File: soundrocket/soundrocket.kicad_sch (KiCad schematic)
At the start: 4 parts, among them J2 XLR3 MALE (OUT), U1 Teensy4.0, U3 CS8406-DSZ

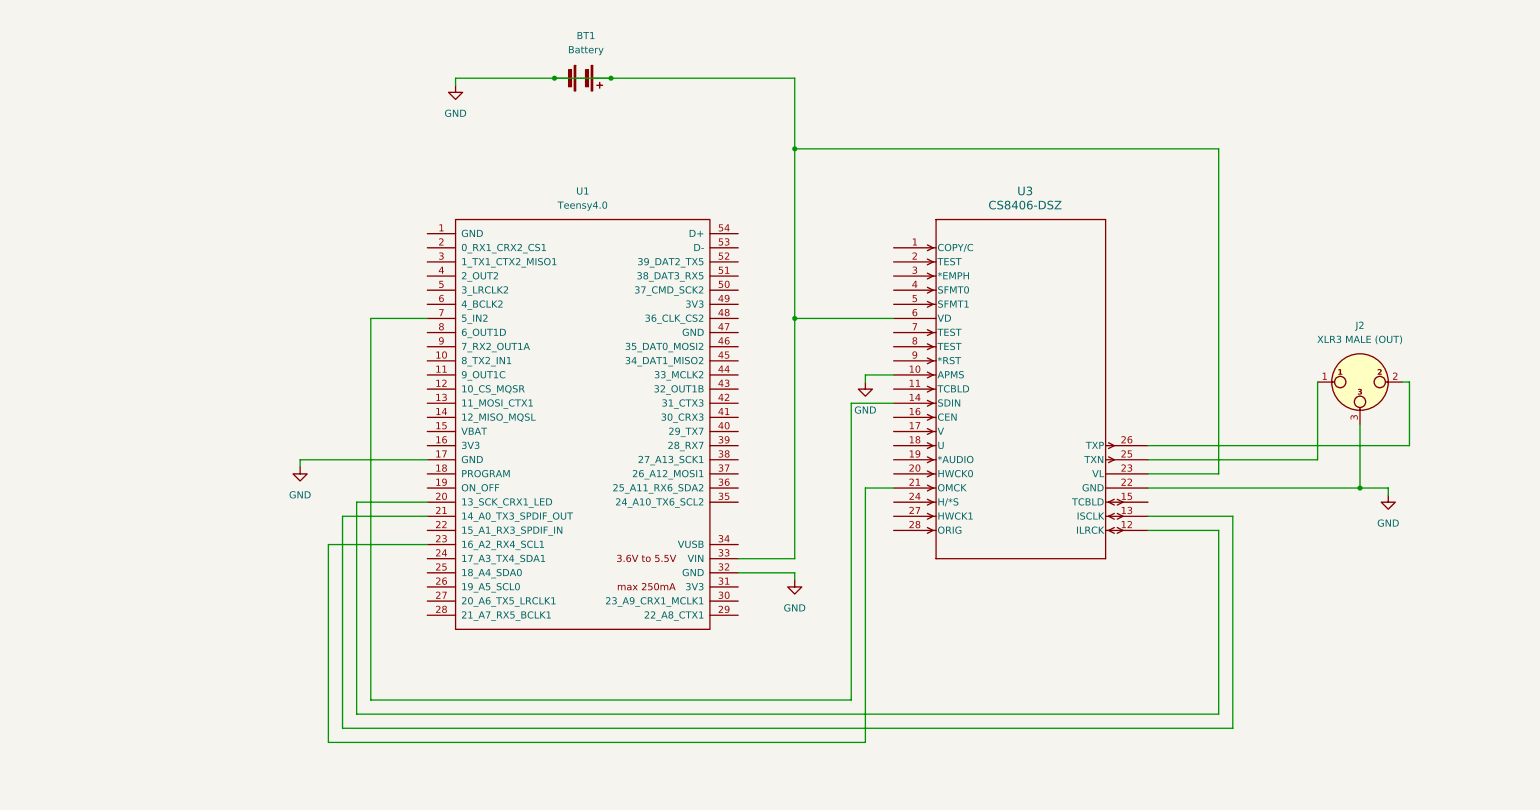
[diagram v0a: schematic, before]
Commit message: Changed to dt4192
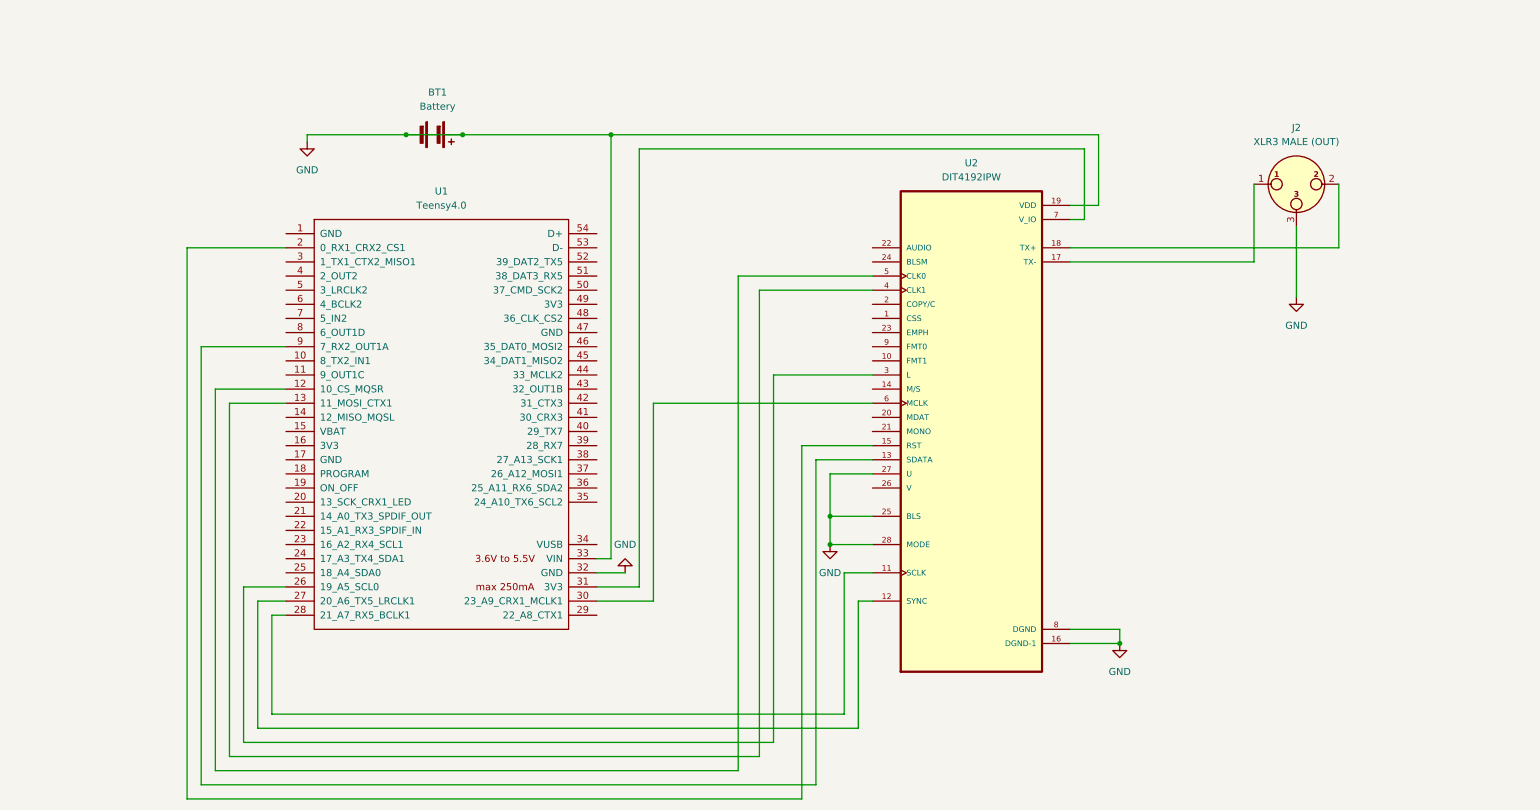
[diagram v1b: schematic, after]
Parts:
- removed U3: CS8406-DSZ, CIR-SOIC-28, symbol 2025-07-12_07-32-56:CS8406-DSZ
- added U2: DIT4192IPW, DIT4192IPW:SOP65P640X120-28N, symbol DIT4192IPW:DIT4192IPW
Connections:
- net GND: now also U2.16 (DGND-1), U2.19 (VDD), U2.25 (BLS), U2.27 (U), U2.28 (MODE), U2.8 (DGND); no longer U1.17 (GND)
- net at J2.1: now also U2.17 (TX-)
- net at J2.2: now also U2.18 (TX+)
- net at U1.12 (10_CS_MQSR): now also U2.5 (CLK0)
- net at U1.13 (11_MOSI_CTX1): now also U2.4 (CLK1)
- net at U1.2 (0_RX1_CRX2_CS1): now also U2.15 (RST)
- net at U1.26 (19_A5_SCL0): now also U2.3 (L)
- net at U1.27 (20_A6_TX5_LRCLK1): now also U2.12 (SYNC)
- net at U1.28 (21_A7_RX5_BCLK1): now also U2.11 (SCLK)
- net at U1.30 (23_A9_CRX1_MCLK1): now also U2.6 (MCLK)
- net at U1.31 (3V3): now also U2.7 (V_IO)
- net at U1.9 (7_RX2_OUT1A): now also U2.13 (SDATA)
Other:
- company: (none) -> Daniel Anderson
- title: (none) -> Sound Rocket
- moved on the sheet: BT1, J2, U1

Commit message: Update Kicad to 9.0
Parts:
- added T1: PE-65612NL, PE-65612NL:XFMR_PE-65612NL, symbol PE-65612NL:PE-65612NL
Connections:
- net at U2.17 (TX-): now also T1.1; no longer J2.1
- net at U2.18 (TX+): now also T1.2; no longer J2.2
- new net: J2.2, T1.3
- new net: J2.1, T1.4
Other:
- moved on the sheet: J2

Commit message: work
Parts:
- added SW1: SW_Push, symbol Switch:SW_Push
- added SW2: RotaryEncoder_Switch, symbol Device:RotaryEncoder_Switch
- renumbered J2 to J1
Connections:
- net GND: now also SW1.1, SW2.C, SW2.S1
- net at U1.4 (2_OUT2): now also SW1.2
- net at U1.5 (3_LRCLK2): now also SW2.S2
- net at U1.7 (5_IN2): now also SW2.B
- net at U1.8 (6_OUT1D): now also SW2.A
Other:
- note added: "UI"

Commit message: schematic start
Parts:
- J1: footprint (none) -> Connector_Audio:Jack_XLR_Neutrik_NC3FAAH-0_Horizontal
- SW1: footprint (none) -> Button_Switch_THT:SW_PUSH-12mm
- SW2: footprint (none) -> Rotary_Encoder:RotaryEncoder_Bourns_Vertical_PEC12R-3x17F-Sxxxx
- U1: footprint (none) -> KiCad Models:Teensy40
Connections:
- net DIT4192-TX-: now reaches T1.1, U2.17 (TX-)
- net DIT4192-TX-: now also J1.2, T1.3
- net DIT4192-TX+: now reaches T1.2, U2.18 (TX+)
- net DIT4192-TX+: now also J1.1, T1.4
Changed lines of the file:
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@@
+		)
+	)
+	(label "DIT4192-TX+"
+		(at 252.73 44.45 0)
+		(effects
+			(font
+				(size 1.27 1.27)
+			)
+			(justify left bottom)
+		)
+	)
+	(label "DIT4192-TX-"
+		(at 267.97 44.45 0)
+		(effects
+			(font
+				(size 1.27 1.27)
+			)
+			(justify left bottom)
+		)
+	)
+	(label "DIT4192-TX+"
+		(at 210.82 55.88 0)
+		(effects
+			(font
+				(size 1.27 1.27)
+			)
+			(justify left bottom)
+		)
+	)
+	(label "DIT4192-TX-"
+		(at 210.82 62.23 0)
+		(effects
+			(font
+				(size 1.27 1.27)
+			)
+			(justify left bottom)
 		)
 	)
@@
 			)
 		)
-		(property "Footprint" ""
+		(property "Footprint" "Button_Switch_THT:SW_PUSH-12mm"
 			(at 27.94 33.02 0)
 			(effects
@@
 			)
 		)
-		(property "Footprint" ""
+		(property "Footprint" "Rotary_Encoder:RotaryEncoder_Bourns_Vertical_PEC12R-3x17F-Sxxxx"
 			(at 24.13 54.356 0)
 			(effects
@@
 			)
 		)
-		(property "Footprint" ""
+		(property "Footprint" "Connector_Audio:Jack_XLR_Neutrik_NC3FAAH-0_Horizontal"
 			(at 260.35 44.45 0)
 			(effects
@@
 			)
 		)
-		(property "Footprint" ""
+		(property "Footprint" "KiCad Models:Teensy40"
 			(at 78.74 82.55 0)
 			(effects

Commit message: Getting close to final
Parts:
- added C1, C2: C_Small, KiCad Models:CAPRR254W54L381T254H466, symbol Device:C_Small
- T1: footprint PE-65612NL:XFMR_PE-65612NL -> PE_65612NL:XFMR_PE-65612NL
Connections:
- net DIT4192-TX+: no longer J1.1, T1.4
- net DIT4192-TX-: no longer J1.2, T1.3
- net GND: now also C1.2, C2.2
- net at SW2.A, U1.8 (6_OUT1D): now also C1.1
- net at SW2.B, U1.7 (5_IN2): now also C2.1
- new net XLR-TX+: J1.1, T1.4
- new net XLR-TX-: J1.2, T1.3

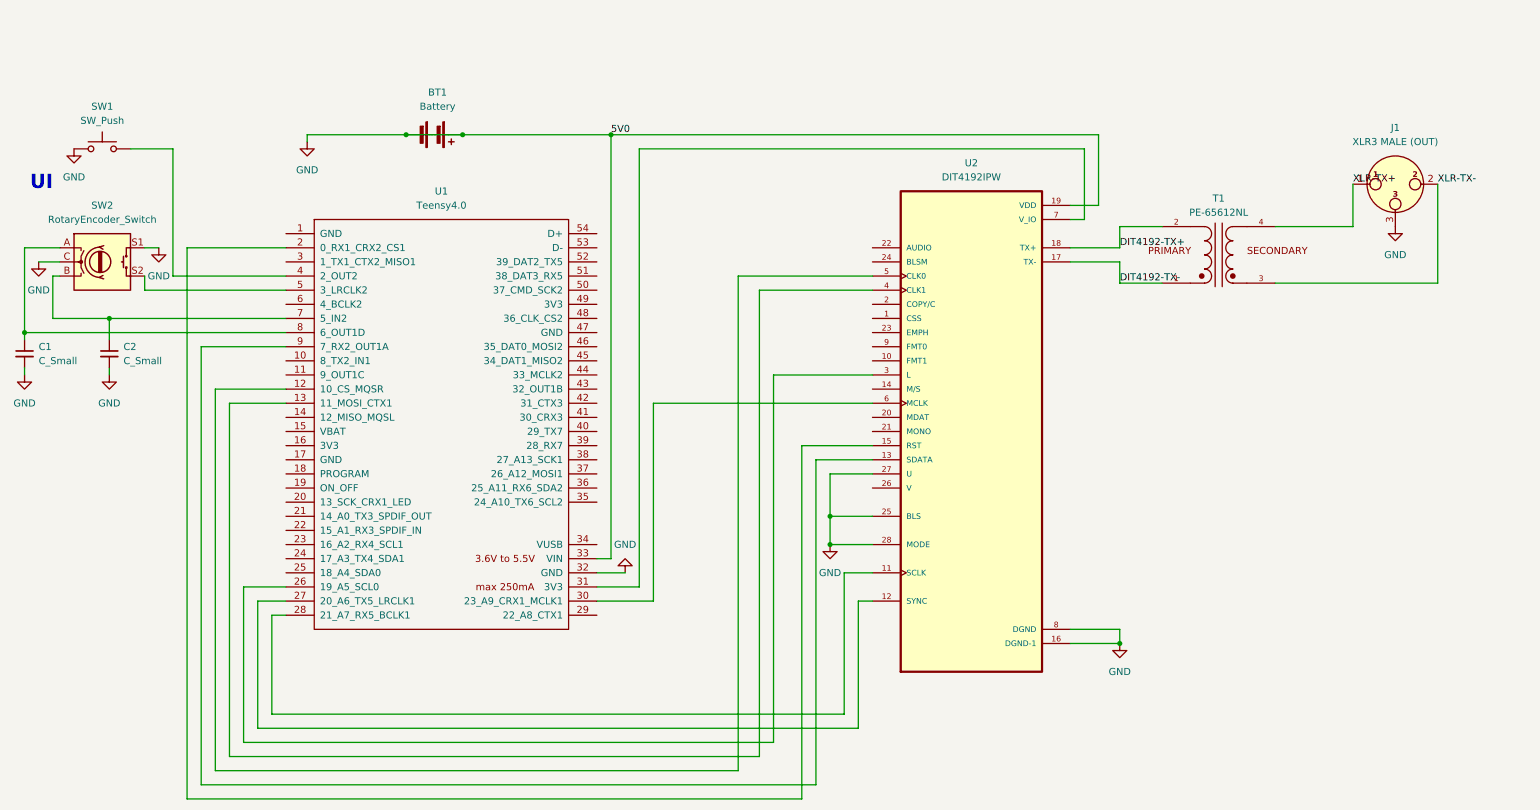
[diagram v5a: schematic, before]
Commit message: Removed /5V0 net
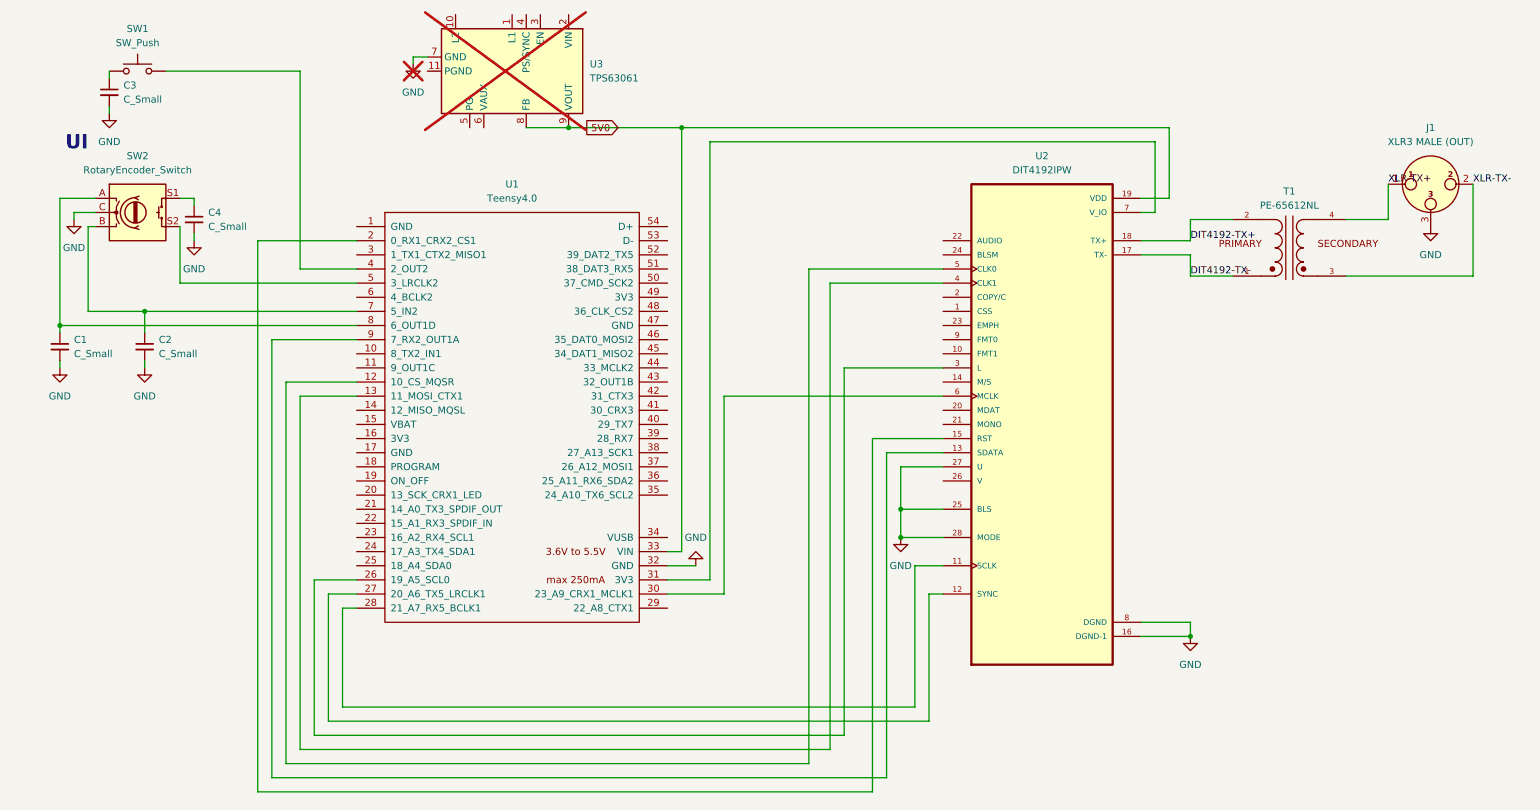
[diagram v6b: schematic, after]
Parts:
- removed BT1: Battery, symbol Device:Battery
- added C3, C4: C_Small, KiCad Models:CAPRR254W54L381T254H466, symbol Device:C_Small
- added U3: TPS63061, Package_SON:Texas_S-PWSON-N10_ThermalVias, symbol Regulator_Switching:TPS63061
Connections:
- net GND: now also C3.2, C4.2, U3.7 (GND); no longer SW1.1, SW2.S1, U1.33 (VIN), U2.19 (VDD)
- new net: C3.1, SW1.1
- new net: C4.1, SW2.S1
- new net 5V0: U1.33 (VIN), U2.19 (VDD), U3.8 (FB), U3.9 (VOUT)
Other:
- moved on the sheet: C1, C2, J1, SW1, SW2, T1, U1, U2

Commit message: soundbullet format
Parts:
- removed J1: XLR3 MALE (OUT), Connector_Audio:Jack_XLR_Neutrik_NC3FAAH-0_Horizontal, symbol Connector_Audio:XLR3
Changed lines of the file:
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@@
-	)
-	(symbol
-		(lib_id "power:GND")
-		(at 266.7 52.07 0)
-		(unit 1)
-		(exclude_from_sim no)
-		(in_bom yes)
-		(on_board yes)
-		(dnp no)
-		(fields_autoplaced yes)
-		(property "Reference" "#PWR03"
-			(at 266.7 58.42 0)
-			(effects
-				(font
-					(size 1.27 1.27)
-				)
-				(hide yes)
-			)
-		)
-		(property "Value" "GND"
-			(at 266.7 57.15 0)
-			(effects
-				(font
-					(size 1.27 1.27)
-				)
-			)
-		)
-		(property "Footprint" ""
-			(at 266.7 52.07 0)
-			(effects
-				(font
-					(size 1.27 1.27)
-				)
-				(hide yes)
-			)
-		)
-		(property "Datasheet" ""
-			(at 266.7 52.07 0)
-			(effects
-				(font
-					(size 1.27 1.27)
-				)
-				(hide yes)
-			)
-		)
-		(property "Description" ""
-			(at 266.7 52.07 0)
-			(effects
-				(font
-					(size 1.27 1.27)
-				)
-			)
-		)
-		(pin "1"
-		)
-		(instances
-			(project "soundrocket"
-				(path "/c2f1f363-3261-4b12-abe7-5fb34db71f7d"
-					(reference "#PWR03")
-					(unit 1)
-				)
-			)
-		)
 	)
 	(symbol
@@
 					(unit 1)
 				)
-			)
-		)
-	)
-	(symbol
-		(lib_id "Connector_Audio:XLR3")
-		(at 266.7 44.45 0)
-		(unit 1)
-		(exclude_from_sim no)
-		(in_bom yes)
-		(on_board yes)
-		(dnp no)
-		(fields_autoplaced yes)
-		(property "Reference" "J1"
-			(at 266.7 34.29 0)
-			(effects
-				(font
-					(size 1.27 1.27)
-				)
-			)
-		)
-		(property "Value" "XLR3 MALE (OUT)"
-			(at 266.7 36.83 0)
-			(effects
-				(font
-					(size 1.27 1.27)
-				)
-			)
-		)
-		(property "Footprint" "Connector_Audio:Jack_XLR_Neutrik_NC3FAAH-0_Horizontal"
-			(at 266.7 44.45 0)
-			(effects
-				(font
-					(size 1.27 1.27)
-				)
-				(hide yes)
-			)
-		)
-		(property "Datasheet" "~"
-			(at 266.7 44.45 0)
-			(effects
-				(font
-					(size 1.27 1.27)
-				)
-				(hide yes)
-			)
-		)
-		(property "Description" ""
-			(at 266.7 44.45 0)
-			(effects
-				(font
-					(size 1.27 1.27)
-				)
-			)
-		)
-		(pin "1"
-		)
-		(pin "3"
-		)
-		(pin "2"
-		)
-		(instances
-			(project "soundrocket"
-				(path "/c2f1f363-3261-4b12-abe7-5fb34db71f7d"
-					(reference "J1")
-					(unit 1)
-				)
